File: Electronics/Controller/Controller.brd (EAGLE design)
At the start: 190 x 90 mm, 25 parts, among them Q1 NDP6020P, U1 GY-521MPU6050, X1 Battery, X2 Switch, X3 Nextion, X4 BUT_L, X5 BUT_R

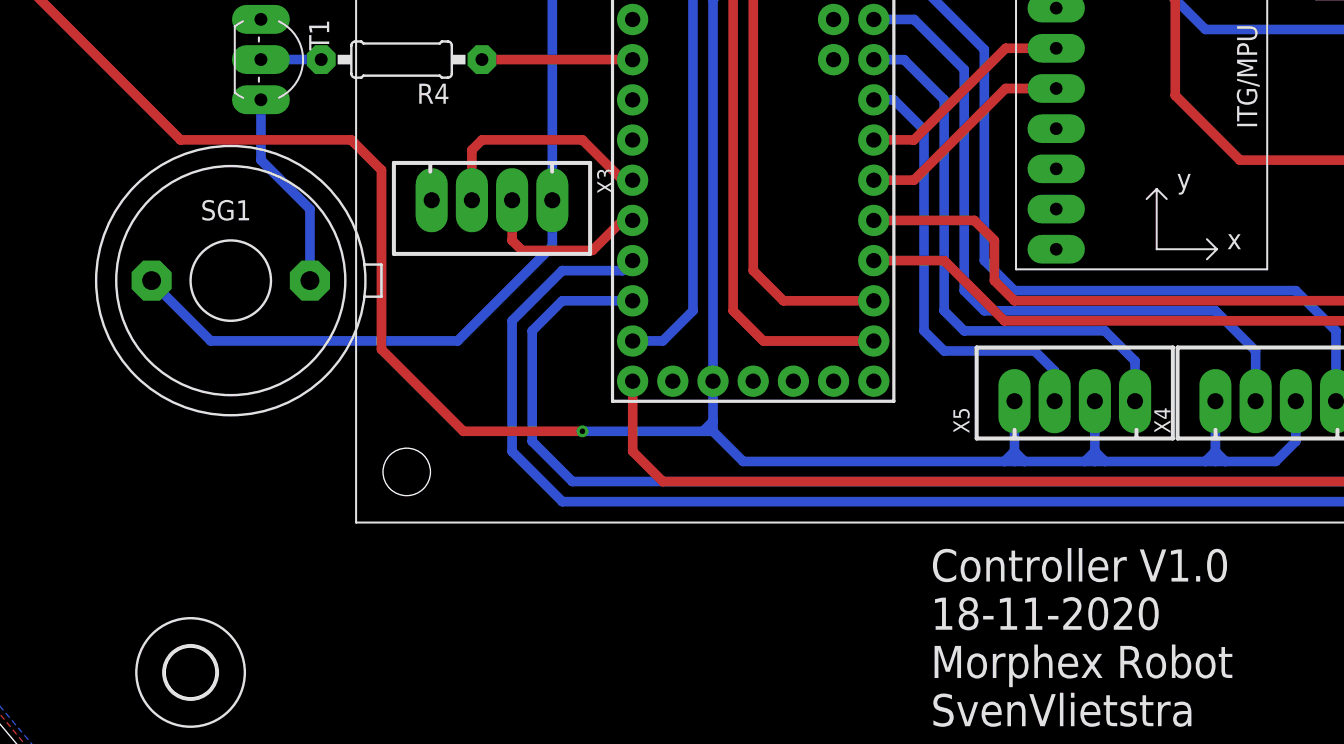
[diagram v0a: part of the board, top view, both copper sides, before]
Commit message: Changed Buzzer
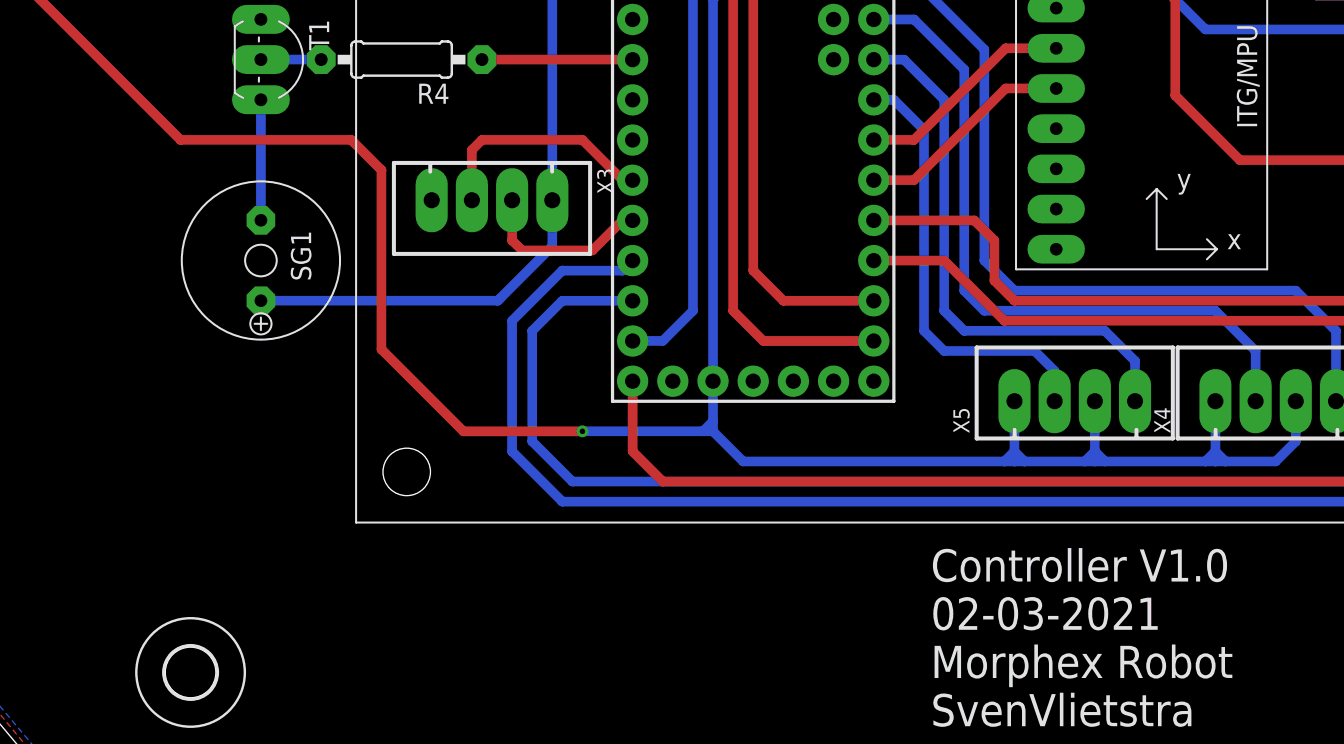
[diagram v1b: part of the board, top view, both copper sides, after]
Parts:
- SG1: value F/EE17P -> Buzzer; device buzzer:F/EE17P -> buzzer:5MM
- moved SG1 2.29 mm to (38.7, 35.6), turned to 270 degrees
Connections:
- net +5V: now also SG1.P$2; no longer SG1.1
- net N$8: now also SG1.P$1; no longer SG1.2
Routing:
- net +5V: track 176.2 -> 166.7 mm
- net N$8: track 12.7 -> 7.62 mm
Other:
- board text added: "Controller V1.0 02-03-2021 Morphex Robot SvenVlietstra"
- board text removed: "Controller V1.0 18-11-2020 Morphex Robot SvenVlietstra"
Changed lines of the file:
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@@
 <?xml version="1.0" encoding="utf-8"?>
 <!DOCTYPE eagle SYSTEM "eagle.dtd">
-<eagle version="9.6.1">
+<eagle version="9.6.2">
 <drawing>
 <settings>
@@
 <plain>
 <text x="81.06586875" y="6.12674375" size="2.032" layer="21" font="vector" ratio="21">Controller V1.0
-18-11-2020
+02-03-2021
 Morphex Robot
 SvenVlietstra</text>
@@
 <attribute name="VALUE" x="123.19" y="69.85" size="1.27" layer="27" rot="R90" align="top-center"/>
 </element>
-<element name="SG1" library="buzzer" library_urn="urn:adsk.eagle:library:113" package="F/EE17P" package3d_urn="urn:adsk.eagle:package:5285/1" value="F/EE17P" x="36.83" y="34.29" smashed="yes">
-<attribute name="MF" value="" x="36.83" y="34.29" size="1.778" layer="27" display="off"/>
-<attribute name="MPN" value="" x="36.83" y="34.29" size="1.778" layer="27" display="off"/>
-<attribute name="NAME" x="34.925" y="38.1" size="1.27" layer="25" ratio="10"/>
-<attribute name="OC_FARNELL" value="unknown" x="36.83" y="34.29" size="1.778" layer="27" display="off"/>
-<attribute name="OC_NEWARK" value="unknown" x="36.83" y="34.29" size="1.778" layer="27" display="off"/>
-<attribute name="POPULARITY" value="0" x="36.83" y="34.29" size="1.778" layer="27" display="off"/>
-<attribute name="VALUE" x="33.655" y="29.21" size="1.27" layer="27" ratio="10"/>
+<element name="SG1" library="buzzer" package="5MM" value="Buzzer" x="38.735" y="35.56" smashed="yes" rot="R270">
+<attribute name="NAME" x="40.64" y="37.465" size="1.27" layer="25" ratio="10" rot="R270"/>
+<attribute name="VALUE" x="35.56" y="38.1" size="1.27" layer="27" ratio="10" rot="R270"/>
 </element>
 <element name="T1" library="transistor" library_urn="urn:adsk.eagle:library:402" package="TO92-EBC" package3d_urn="urn:adsk.eagle:package:29915/2" value="" x="40.005" y="48.26" smashed="yes" rot="R270">
@@
 <contactref element="U$1" pad="VIN"/>
 <contactref element="U$8" pad="OUT+"/>
-<contactref element="SG1" pad="1"/>
-<wire x1="35.56" y1="30.48" x2="51.169284375" y2="30.48" width="0.6096" layer="16"/>
-<wire x1="35.56" y1="30.48" x2="31.8262" y2="34.2138" width="0.6096" layer="16"/>
-<wire x1="31.8262" y1="34.2138" x2="31.8262" y2="34.29" width="0.6096" layer="16"/>
+<contactref element="SG1" pad="P$2"/>
 <wire x1="77.47" y1="60.9557" x2="77.4675" y2="60.9532" width="1.016" layer="16"/>
 <wire x1="96.52" y1="45.992140625" x2="96.52" y2="52.07" width="0.6096" layer="1"/>
@@
 <contactref element="X3" pad="1"/>
 <wire x1="57.15" y1="61.595" x2="57.15" y2="39.37" width="0.6096" layer="16"/>
-<wire x1="51.169284375" y1="30.48" x2="57.15" y2="36.460715625" width="0.6096" layer="16"/>
+<wire x1="53.84214375" y1="33.152859375" x2="57.15" y2="36.460715625" width="0.6096" layer="16"/>
 <wire x1="57.15" y1="36.460715625" x2="57.15" y2="39.37" width="0.6096" layer="16"/>
+<wire x1="38.735" y1="33.02" x2="53.709284375" y2="33.02" width="0.6096" layer="16"/>
+<wire x1="53.709284375" y1="33.02" x2="53.84214375" y2="33.152859375" width="0.6096" layer="16"/>
 </signal>
 <signal name="26/A12/DAC">
@@
 <signal name="N$8">
 <contactref element="T1" pad="C"/>
-<contactref element="SG1" pad="2"/>
-<wire x1="41.8338" y1="34.29" x2="41.8338" y2="38.8112" width="0.6096" layer="16"/>
-<wire x1="41.8338" y1="38.8112" x2="38.735" y2="41.91" width="0.6096" layer="16"/>
-<wire x1="38.735" y1="41.91" x2="38.735" y2="45.72" width="0.6096" layer="16"/>
+<contactref element="SG1" pad="P$1"/>
+<wire x1="38.735" y1="45.72" x2="38.735" y2="38.1" width="0.6096" layer="16"/>
 </signal>
 <signal name="BUZZER">
